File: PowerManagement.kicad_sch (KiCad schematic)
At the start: 22 parts, among them J5 Screw_Terminal_01x02_POWER, U2 XC6210B332MR, U3 XL1509

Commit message: Circular pcb edge cut
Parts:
- J5: footprint Connector_Phoenix_MC:PhoenixContact_MC_1,5_2-G-3.5_1x02_P3.50mm_Horizontal -> Connector_AMASS:AMASS_XT30PW-M_1x02_P2.50mm_Horizontal
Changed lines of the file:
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@@
 			)
 		)
-		(property "Footprint" "Connector_Phoenix_MC:PhoenixContact_MC_1,5_2-G-3.5_1x02_P3.50mm_Horizontal"
+		(property "Footprint" "Connector_AMASS:AMASS_XT30PW-M_1x02_P2.50mm_Horizontal"
 			(at 35.56 39.37 0)
 			(effects

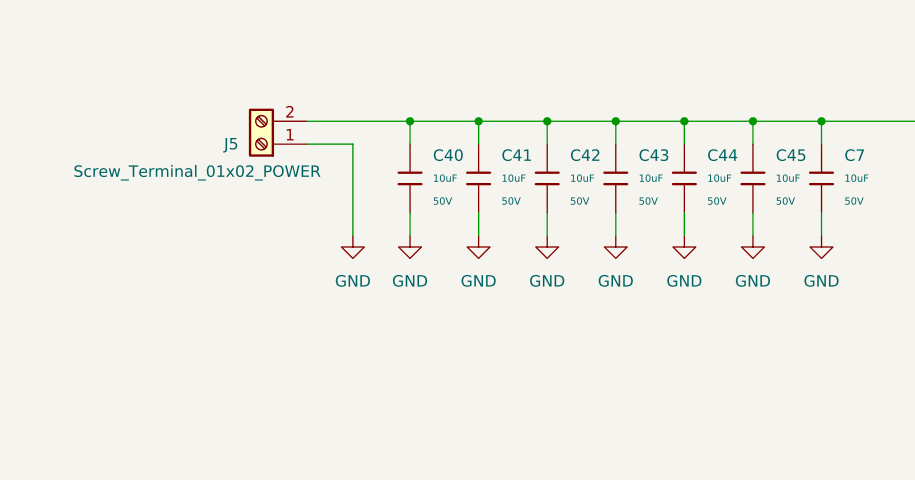
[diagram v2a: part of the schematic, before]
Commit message: Reduced number of 10uF caps
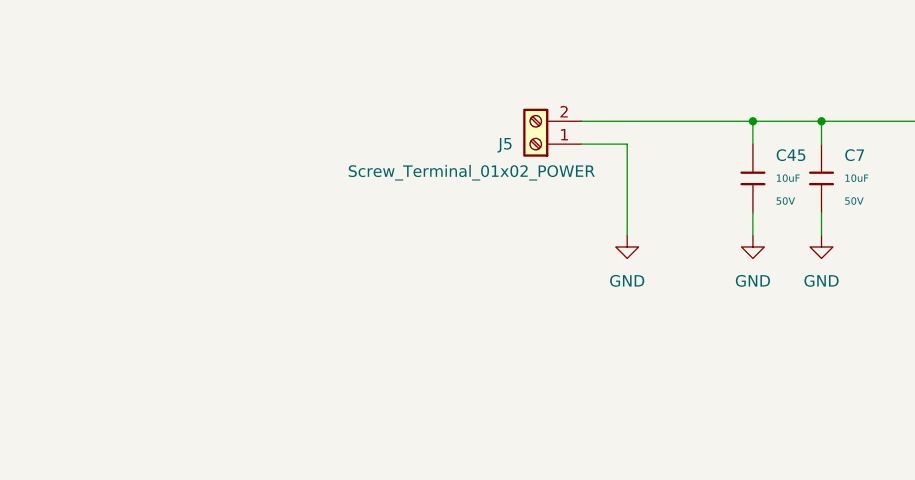
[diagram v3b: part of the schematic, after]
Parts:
- removed C40, C41, C42, C43, C44: 10uF, PCM_JLCPCB:C_1206, symbol PCM_JLCPCB-Capacitors:1206,10uF
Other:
- moved on the sheet: J5

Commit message: DRC check - fine tuning
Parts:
- added J57: C189893, Connector_PinHeader_2.54mm:PinHeader_1x03_P2.54mm_Vertical, symbol Connector_Generic:Conn_01x03
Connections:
- net +3.3V: now also J57.2 (Pin_2)
- net +5V: now also J57.1 (Pin_1)
- net GND: now also J57.3 (Pin_3)

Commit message: Drc, Bom done
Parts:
- J5: LCSC (none) -> C431092
- L1: LCSC (none) -> C96920
- U2: LCSC (none) -> C49375238
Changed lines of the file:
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@@
+			)
+		)
+		(property "LCSC" "C431092"
+			(at 63.5 39.3701 0)
+			(effects
+				(font
+					(size 1.27 1.27)
+				)
+				(hide yes)
 			)
 		)
@@
 			)
 		)
+		(property "LCSC" "C96920"
+			(at 170.18 31.75 0)
+			(effects
+				(font
+					(size 1.27 1.27)
+				)
+				(hide yes)
+			)
+		)
 		(pin "1"
 		)
@@
 			)
 		)
+		(property "LCSC" "C49375238"
+			(at 140.97 86.36 0)
+			(effects
+				(font
+					(size 1.27 1.27)
+				)
+				(hide yes)
+			)
+		)

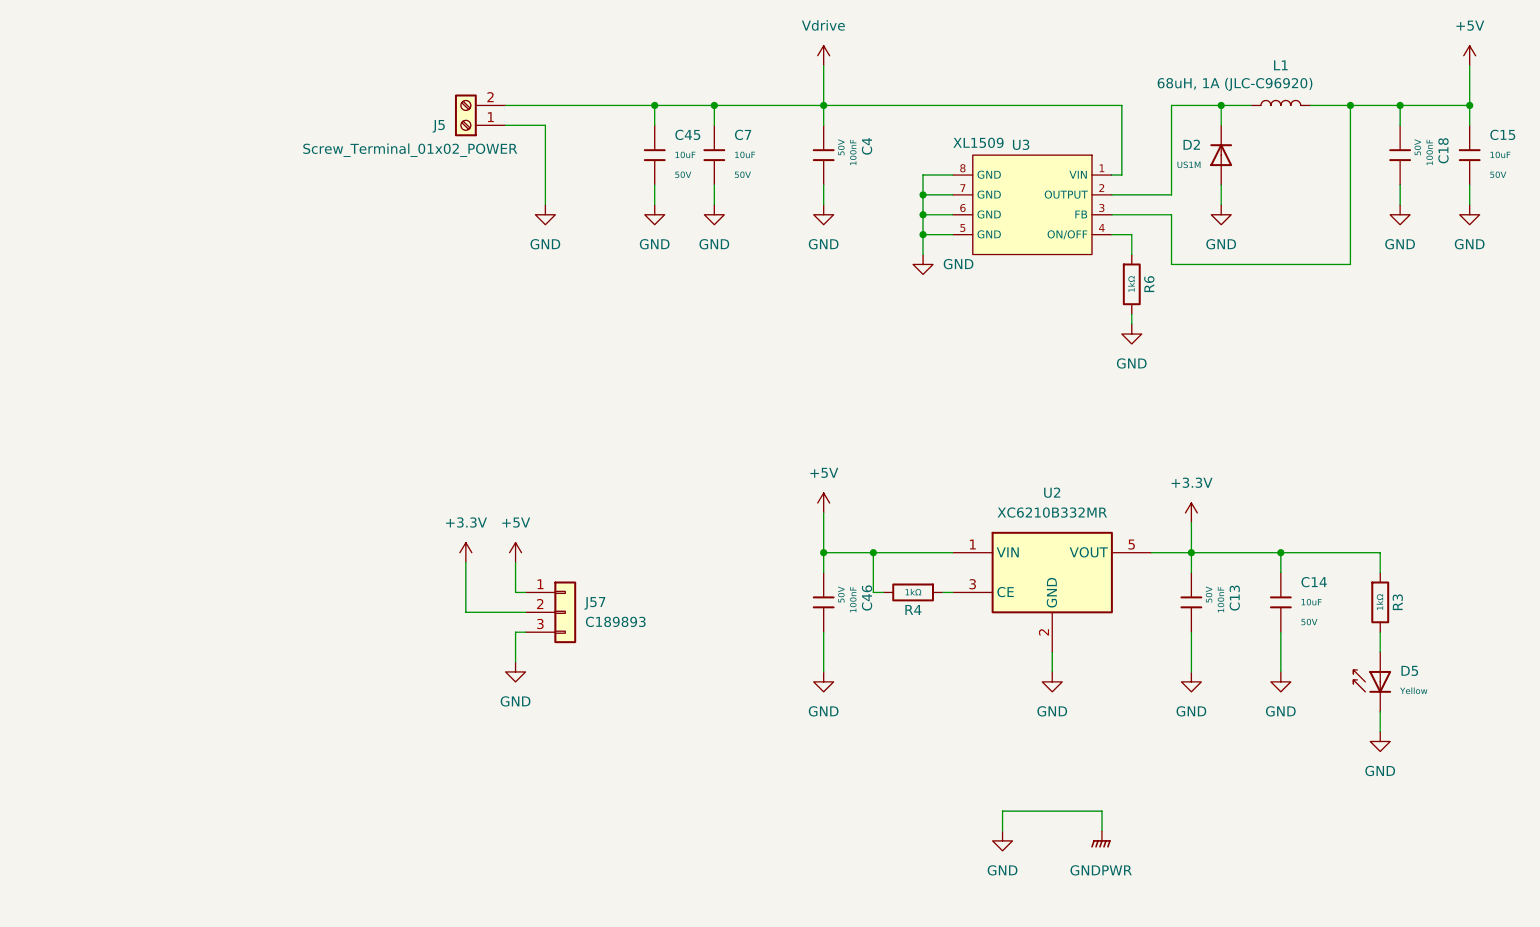
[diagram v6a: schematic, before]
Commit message: Replaced 3.3V linear regulator with switch mode regulator
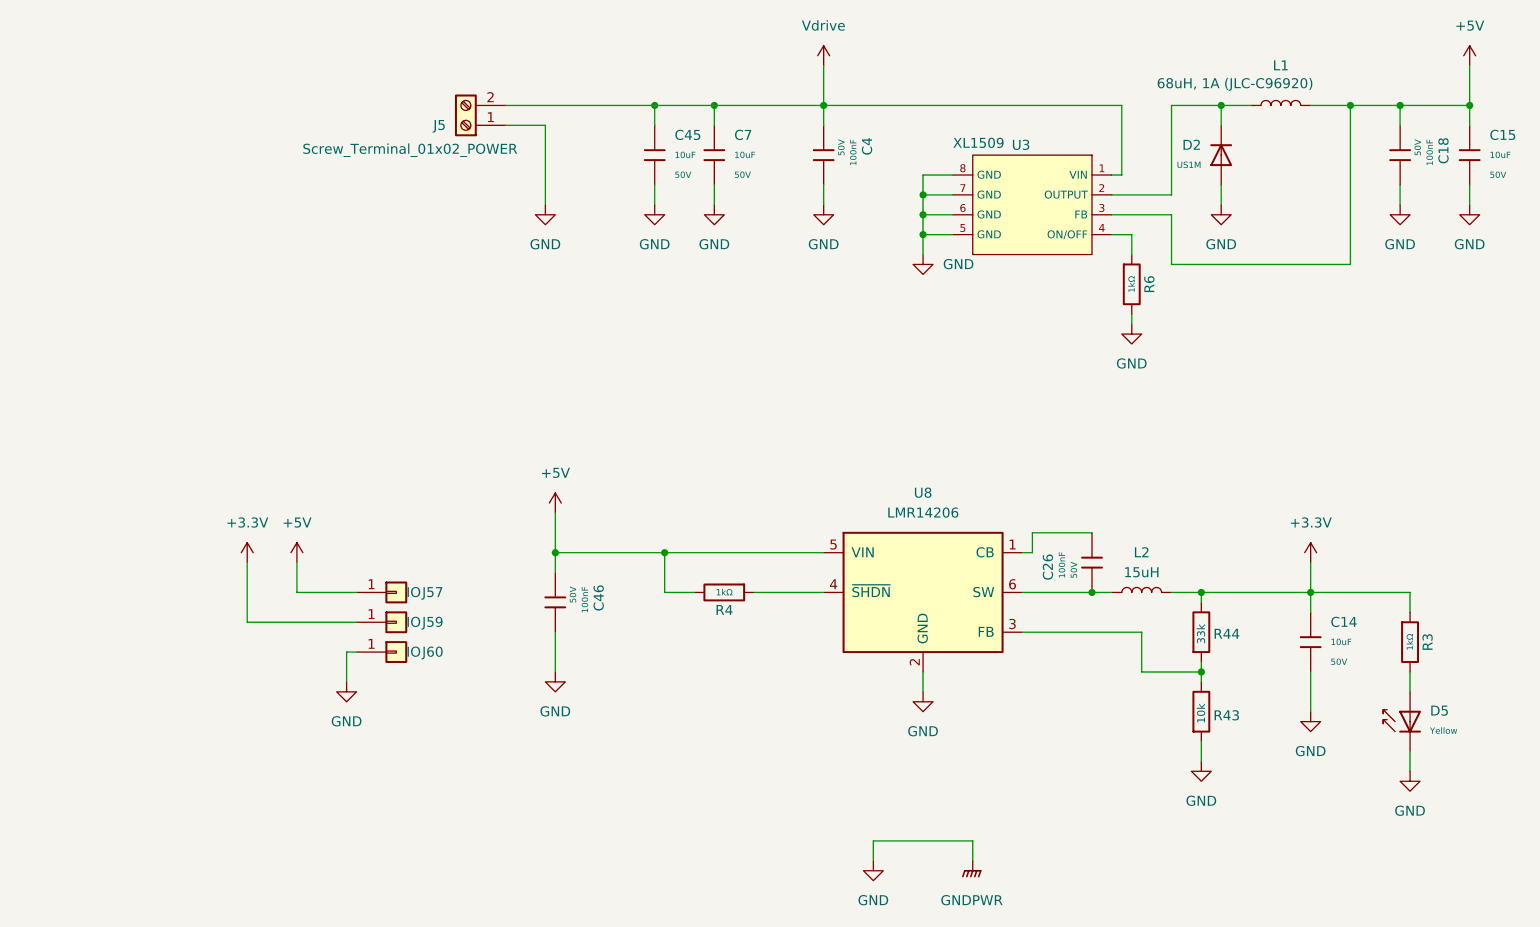
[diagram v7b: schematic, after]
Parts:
- removed C13: 100nF, PCM_JLCPCB:C_0603, symbol PCM_JLCPCB-Capacitors:0603,100nF
- removed J57: C189893, Connector_PinHeader_2.54mm:PinHeader_1x03_P2.54mm_Vertical, symbol Connector_Generic:Conn_01x03
- removed U2: XC6210B332MR, Package_TO_SOT_SMD:SOT-23-5, symbol Regulator_Linear:XC6210B332MR
- added C26: 100nF, PCM_JLCPCB:C_0603, symbol PCM_JLCPCB-Capacitors:0603,100nF
- added J57, J59, J60: IO, TestPoint:TestPoint_THTPad_D1.0mm_Drill0.5mm, symbol Connector_Generic:Conn_01x01
- added L2: 15uH, Inductor_SMD:L_Changjiang_FNR3021S, symbol Device:L
- added R43: 10k, PCM_JLCPCB:R_0603, symbol Device:R
- added R44: 33k, PCM_JLCPCB:R_0603, symbol Device:R
- added U8: LMR14206, Package_TO_SOT_SMD:SOT-23-6, symbol Regulator_Switching:LMR14206
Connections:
- net +3.3V: now also J59.1 (Pin_1), L2.2, R44.1
- net +5V: now also J57.1 (Pin_1), U8.5 (VIN)
- net GND: now also J60.1 (Pin_1), R43.2, U8.2 (GND)
- net at R4.1: now also U8.4 (~{SHDN})
- new net: C26.1, L2.1, U8.6 (SW)
- new net: R43.1, R44.2, U8.3 (FB)
- new net: C26.2, U8.1 (CB)
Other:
- moved on the sheet: C14, C46, D5, R3, R4
